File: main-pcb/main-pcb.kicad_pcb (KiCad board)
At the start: 10 copper layers, 118 x 90 mm, 443 parts, among them J1 CONN_01X03, J10 CONN_DUMPTRUCK_HOST, J11 CONN_01X03, J12 PMOD_HOST, J13 PMOD_HOST, J14 USB_C_Receptacle_USB2.0, J2 CORTEX_DEBUG_ETM, J3 XILINX_JTAG, J4 CORTEX_DEBUG_ETM, J5 CONN_01X03, J6 0826-1G1T-23-F, J7 CONN_DUMPTRUCK_HOST, J8 CONN_DUMPTRUCK_HOST, J9 CONN_DUMPTRUCK_HOST, M1 MECHANICAL, M2 SCREWHOLE, M3 SCREWHOLE, M4 SCREWHOLE, M5 SCREWHOLE, M6 MECHANICAL, M7 MECHANICAL, M8 MECHANICAL, M9 MECHANICAL, Q1 SSM6N58NU, SW1 SWITCH, SW2 SWITCH, U1 XC7S100-1FGGA484C, U10 NCP45525IMNTWG-H, U11 LTC3374-QFN, U12 AT24MAC402, U13 ECS-1612MV-250-CN, U14 STM32H735-UFBGA176-25, U15 S27KL0642GABHB020, U16 ECS-1612MV-250-CN, U17 S27KS0642GABHI030, U18 ECS-1612MV-250-CN, U19 INA230, U2 STM32L431-QFN48, U20 KSZ9031RN, U21 RCLAMP0514M, U22 RCLAMP0514M, U23 NCP45525IMNTWG-H, U24 IS25WP256D-JLLE, U25 INA230, U26 74LVC1T45, U27 NCP45525IMNTWG-H, U28 INA230, U29 NCP45525IMNTWG-H, U3 INA230, U30 INA230, U31 NCP45525IMNTWG-H, U32 INA230, U33 19-C47/RSGHBHC-5V01/2T, U34 19-C47/RSGHBHC-5V01/2T, U35 19-C47/RSGHBHC-5V01/2T, U36 19-C47/RSGHBHC-5V01/2T, U37 19-C47/RSGHBHC-5V01/2T, U38 19-C47/RSGHBHC-5V01/2T, U39 NCP45525IMNTWG-H, U4 INA230, U5 INA230, U6 INA230, U7 INA230, U8 INA230, U9 INA230

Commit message: 1088 unrouted
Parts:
- moved C145 45.4 mm to (196.8, 76.5)
- moved C146 45.4 mm to (196.8, 78.0)
- moved C151 45.4 mm to (196.8, 79.5)
- moved C152 45.4 mm to (196.8, 81.0)
- moved C157 45.4 mm to (199.2, 75.0)
- moved C158 45.4 mm to (199.2, 76.5)
- moved C159 45.4 mm to (199.2, 78.0)
- moved C160 45.4 mm to (199.2, 79.5)
- moved C161 45.4 mm to (199.2, 81.0)
- moved R45 45.4 mm to (201.8, 76.5)
- moved R47 45.4 mm to (201.8, 78.0)
- moved R48 45.4 mm to (201.8, 79.5)
- moved R49 45.4 mm to (201.8, 81.0)
- moved R54 45.4 mm to (204.2, 75.0)
- moved R55 45.4 mm to (204.2, 76.5)
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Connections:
- U1 pad A10: /2V5 VCCIO socket/DUT_GPIO4 -> /2V5 VCCIO socket/DUT_GPIO32
- U1 pad A2: /2V5 VCCIO socket/DUT_GPIO30 -> /2V5 VCCIO socket/DUT_GPIO25
- U1 pad A3: /2V5 VCCIO socket/DUT_GPIO28 -> /2V5 VCCIO socket/DUT_GPIO21
- U1 pad A4: /2V5 VCCIO socket/DUT_GPIO27 -> /2V5 VCCIO socket/DUT_GPIO24
- U1 pad A5: /2V5 VCCIO socket/DUT_GPIO26 -> /2V5 VCCIO socket/DUT_GPIO28
- U1 pad A6: /2V5 VCCIO socket/DUT_GPIO8 -> /2V5 VCCIO socket/DUT_GPIO46
- U1 pad A7: /2V5 VCCIO socket/DUT_GPIO7 -> /2V5 VCCIO socket/DUT_GPIO42
- U1 pad A9: /2V5 VCCIO socket/DUT_GPIO2 -> /2V5 VCCIO socket/DUT_GPIO36
- U1 pad B1: /2V5 VCCIO socket/DUT_GPIO34 -> /2V5 VCCIO socket/DUT_GPIO47
- U1 pad B10: /2V5 VCCIO socket/DUT_GPIO3 -> /2V5 VCCIO socket/DUT_GPIO30
- U1 pad B2: /2V5 VCCIO socket/DUT_GPIO33 -> /2V5 VCCIO socket/DUT_GPIO49
- U1 pad B3: /2V5 VCCIO socket/DUT_GPIO29 -> /2V5 VCCIO socket/DUT_GPIO23
- U1 pad B6: /2V5 VCCIO socket/DUT_GPIO25 -> /2V5 VCCIO socket/DUT_GPIO44
- U1 pad B7: /2V5 VCCIO socket/DUT_GPIO10 -> /2V5 VCCIO socket/DUT_GPIO40
- U1 pad B8: /2V5 VCCIO socket/DUT_GPIO9 -> /2V5 VCCIO socket/DUT_GPIO38
- U1 pad B9: /2V5 VCCIO socket/DUT_GPIO1 -> /2V5 VCCIO socket/DUT_GPIO34
- U1 pad C1: /2V5 VCCIO socket/DUT_GPIO36 -> /2V5 VCCIO socket/DUT_GPIO43
- U1 pad C2: /2V5 VCCIO socket/DUT_GPIO35 -> /2V5 VCCIO socket/DUT_GPIO45
- U1 pad C3: /2V5 VCCIO socket/DUT_GPIO32 -> /2V5 VCCIO socket/DUT_GPIO22
- U1 pad C4: /2V5 VCCIO socket/DUT_GPIO31 -> /2V5 VCCIO socket/DUT_GPIO26
- U1 pad C5: /2V5 VCCIO socket/DUT_GPIO14 -> /2V5 VCCIO socket/DUT_GPIO48
- U1 pad C6: /2V5 VCCIO socket/DUT_GPIO13 -> /2V5 VCCIO socket/DUT_GPIO10
- U1 pad C8: /2V5 VCCIO socket/DUT_GPIO6 -> /2V5 VCCIO socket/DUT_GPIO16
- U1 pad C9: /2V5 VCCIO socket/DUT_GPIO5 -> /2V5 VCCIO socket/DUT_GPIO20
- U1 pad D1: /2V5 VCCIO socket/DUT_GPIO48 -> /2V5 VCCIO socket/DUT_GPIO39
- U1 pad D2: /2V5 VCCIO socket/DUT_GPIO46 -> /2V5 VCCIO socket/DUT_GPIO41
- U1 pad D4: /2V5 VCCIO socket/DUT_GPIO40 -> /2V5 VCCIO socket/DUT_GPIO15
- U1 pad D5: /2V5 VCCIO socket/DUT_GPIO16 -> /2V5 VCCIO socket/DUT_GPIO17
- U1 pad D6: /2V5 VCCIO socket/DUT_GPIO15 -> /2V5 VCCIO socket/DUT_GPIO8
- U1 pad D8: /2V5 VCCIO socket/DUT_GPIO11 -> /2V5 VCCIO socket/DUT_GPIO14
- U1 pad E1: /2V5 VCCIO socket/DUT_GPIO42 -> /2V5 VCCIO socket/DUT_GPIO35
- U1 pad E2: /2V5 VCCIO socket/DUT_GPIO47 -> /2V5 VCCIO socket/DUT_GPIO33
- U1 pad E3: /2V5 VCCIO socket/DUT_GPIO45 -> /2V5 VCCIO socket/DUT_GPIO37
- U1 pad E4: /2V5 VCCIO socket/DUT_GPIO39 -> /2V5 VCCIO socket/DUT_GPIO11
- U1 pad E5: /2V5 VCCIO socket/DUT_GPIO20 -> /2V5 VCCIO socket/DUT_GPIO13
- U1 pad E8: /2V5 VCCIO socket/DUT_GPIO0 -> /2V5 VCCIO socket/DUT_GPIO18
- U1 pad F1: /2V5 VCCIO socket/DUT_GPIO41 -> /2V5 VCCIO socket/DUT_GPIO31
- U1 pad F4: /2V5 VCCIO socket/DUT_GPIO49 -> /2V5 VCCIO socket/DUT_GPIO9
- U1 pad F6: /2V5 VCCIO socket/DUT_GPIO24 -> /2V5 VCCIO socket/DUT_GPIO4
- U1 pad F7: /2V5 VCCIO socket/DUT_GPIO23 -> /2V5 VCCIO socket/DUT_GPIO2
- U1 pad F8: /2V5 VCCIO socket/DUT_GPIO18 -> /2V5 VCCIO socket/DUT_GPIO0
- U1 pad G1: /2V5 VCCIO socket/DUT_GPIO44 -> /2V5 VCCIO socket/DUT_GPIO27
- U1 pad G2: /2V5 VCCIO socket/DUT_GPIO43 -> /2V5 VCCIO socket/DUT_GPIO29
- U1 pad G3: /2V5 VCCIO socket/DUT_GPIO38 -> /2V5 VCCIO socket/DUT_GPIO5
- U1 pad G4: /2V5 VCCIO socket/DUT_GPIO37 -> /2V5 VCCIO socket/DUT_GPIO7
- U1 pad G6: /2V5 VCCIO socket/DUT_GPIO22 -> /2V5 VCCIO socket/DUT_GPIO3
- U1 pad G7: /2V5 VCCIO socket/DUT_GPIO21 -> /2V5 VCCIO socket/DUT_GPIO1
- U1 pad G8: /2V5 VCCIO socket/DUT_GPIO17 -> /2V5 VCCIO socket/DUT_GPIO6
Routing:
- net /2V5 VCCIO socket/DUT_GPIO18: track 0.00 -> 42.8 mm, vias 0 -> 2
- net /2V5 VCCIO socket/DUT_GPIO8: track 1.00 -> 43.6 mm, vias 0 -> 2
- net /2V5 VCCIO socket/DUT_GPIO30: track 1.00 -> 43.0 mm
- net /2V5 VCCIO socket/DUT_GPIO3: track 2.71 -> 44.4 mm, vias 0 -> 2
- net /2V5 VCCIO socket/DUT_GPIO10: track 2.46 -> 42.2 mm, vias 0 -> 2
- net /2V5 VCCIO socket/DUT_GPIO12: track 2.96 -> 42.5 mm, vias 1 -> 2
- net /2V5 VCCIO socket/DUT_GPIO14: track 3.21 -> 42.5 mm, vias 0 -> 2
- net /2V5 VCCIO socket/DUT_GPIO7: track 1.00 -> 39.6 mm, vias 0 -> 2
- net /2V5 VCCIO socket/DUT_GPIO5: track 3.25 -> 40.3 mm, vias 1 -> 2
- net /2V5 VCCIO socket/DUT_GPIO32: track 3.21 -> 39.8 mm
- net /2V5 VCCIO socket/DUT_GPIO16: track 4.66 -> 41.1 mm, vias 1 -> 2
- net /2V5 VCCIO socket/DUT_GPIO20: track 4.71 -> 40.7 mm, vias 1 -> 2
- net /2V5 VCCIO socket/DUT_GPIO9: track 2.71 -> 38.4 mm, vias 0 -> 2
- net /2V5 VCCIO socket/DUT_GPIO13: track 1.75 -> 36.6 mm, vias 1 -> 2
- net /2V5 VCCIO socket/DUT_GPIO17: track 0.00 -> 34.7 mm, vias 0 -> 2
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
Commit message: Continued routing
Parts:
- C20, C39: moved to B.Cu
- moved C178 172.4 mm to (23.2, 38.4)
- moved C179 172.4 mm to (27.0, 37.2)
- moved C180 172.4 mm to (27.0, 38.8)
- moved C181 172.4 mm to (27.0, 40.2)
- moved C182 172.4 mm to (23.2, 42.3)
- moved R94 172.4 mm to (27.0, 41.8)
- moved R95 172.4 mm to (27.0, 43.2)
- moved U23 172.4 mm to (30.1, 42.9)
- moved U25 172.4 mm to (30.6, 38.9)
- moved U36 135.8 mm to (31.7, 100.0)
- moved C204 130.1 mm to (31.4, 96.7)
- moved C209 123.8 mm to (73.2, 89.2), turned to -90 degrees
- moved TP13 123.7 mm to (59.8, 90.2)
- moved C210 120.6 mm to (76.5, 88.0), turned to 180 degrees
- moved C211 114.5 mm to (81.5, 95.8), turned to -135 degrees
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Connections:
- U1 pad F6: /2V5 VCCIO socket/DUT_GPIO4 -> /2V5 VCCIO socket/DUT_GPIO2
- U1 pad F7: /2V5 VCCIO socket/DUT_GPIO2 -> /2V5 VCCIO socket/DUT_GPIO4
- U1 pad F8: /2V5 VCCIO socket/DUT_GPIO0 -> /2V5 VCCIO socket/DUT_GPIO6
- U1 pad G8: /2V5 VCCIO socket/DUT_GPIO6 -> /2V5 VCCIO socket/DUT_GPIO0
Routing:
- net /GND: track 863.3 -> 934.1 mm, vias 233 -> 266
- net /2V5 VCCIO socket/DUT_GPIO0: track 0.00 -> 49.3 mm, vias 0 -> 2
- net /2V5 VCCIO socket/DUT_GPIO4: track 0.00 -> 46.2 mm, vias 0 -> 2
- net /2V5 VCCIO socket/DUT_GPIO2: track 0.00 -> 46.1 mm, vias 0 -> 2
- net /2V5 VCCIO socket/DUT_GPIO6: track 0.00 -> 46.0 mm, vias 0 -> 2
- net /2V5 VCCIO socket/DUT_GPIO1: track 0.00 -> 45.3 mm, vias 0 -> 2
- net /1V2: track 99.4 -> 119.2 mm, vias 8 -> 14
- net /1V0: track 64.7 -> 75.8 mm, vias 16 -> 28
- net /2V5: track 31.4 -> 38.5 mm, vias 4 -> 6
- net /1V8: track 164.1 -> 169.8 mm, vias 36 -> 43
- net /3V3: track 225.5 -> 230.9 mm, vias 15 -> 17
- net /2V5 VCCIO socket/DUT_GPIO20: track 40.7 -> 42.2 mm
- net /2V5 VCCIO socket/DUT_GPIO18: track 42.8 -> 44.3 mm
- net /Ethernet/FPGA_RAM_DQ6: track 19.2 -> 17.9 mm
- net /Ethernet/FPGA_RAM_DQ7: track 15.6 -> 14.6 mm
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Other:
- board text added: "1.2V IO"
- board text added: "1.8V IO"
- board text added: "1V2"
- board text added: "2.5V IO"
- board text added: "3.3V IO"
- board text added: "3V3"
- board text added: "FPGA JTAG"
- board text added: "FPGA PMOD"
- board text added: "GND"
- board text added: "MCU BOOT0"
- board text added: "MCU I2C"
- board text added: "MCU JTAG"
- board text added: "MCU PMOD"
- board text added: "MCU UART"
- board text added: "RX"
- board text added: "SCL"
- board text added: "SDA"
- board text added: "SUPER JTAG"
- board text added: "SUPER UART"
- board text added: "TX"
- board text added: "USB PWR 5V 900 mA"

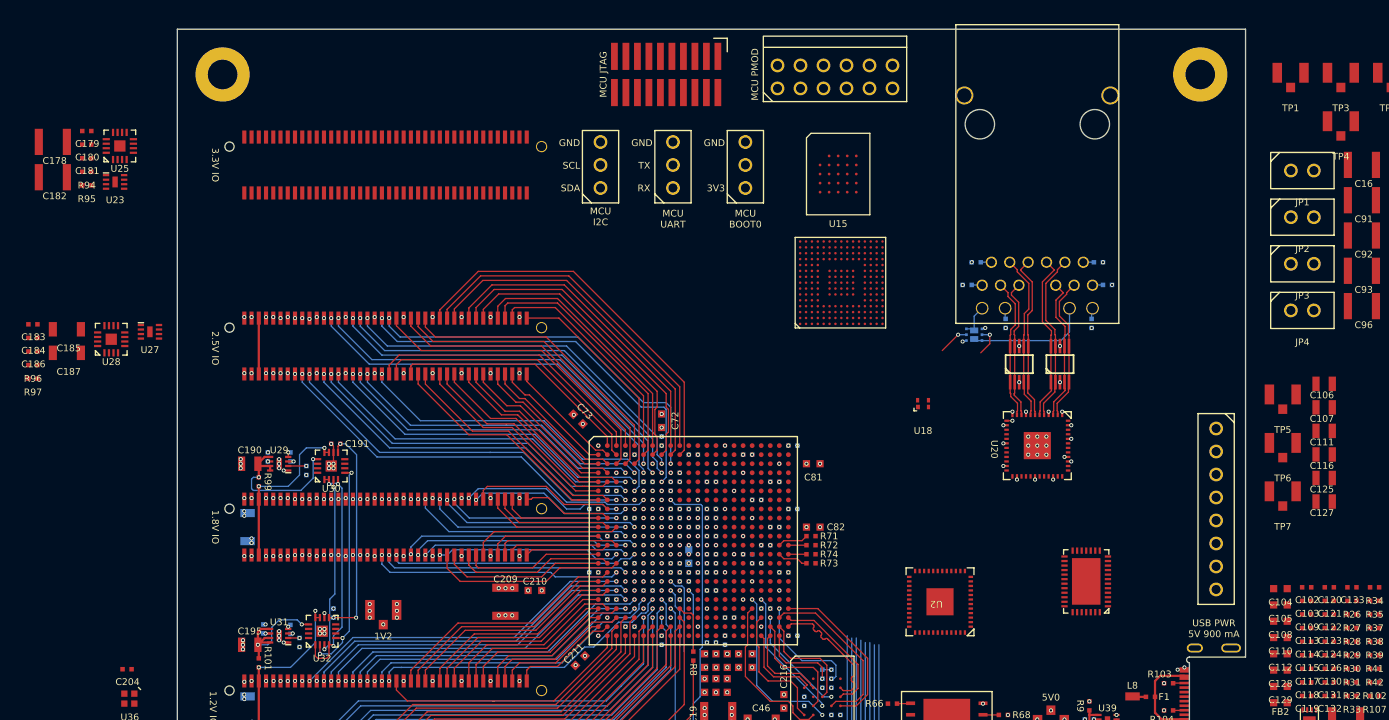
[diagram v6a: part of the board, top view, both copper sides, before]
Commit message: Continued routing 3V3 DUT socket
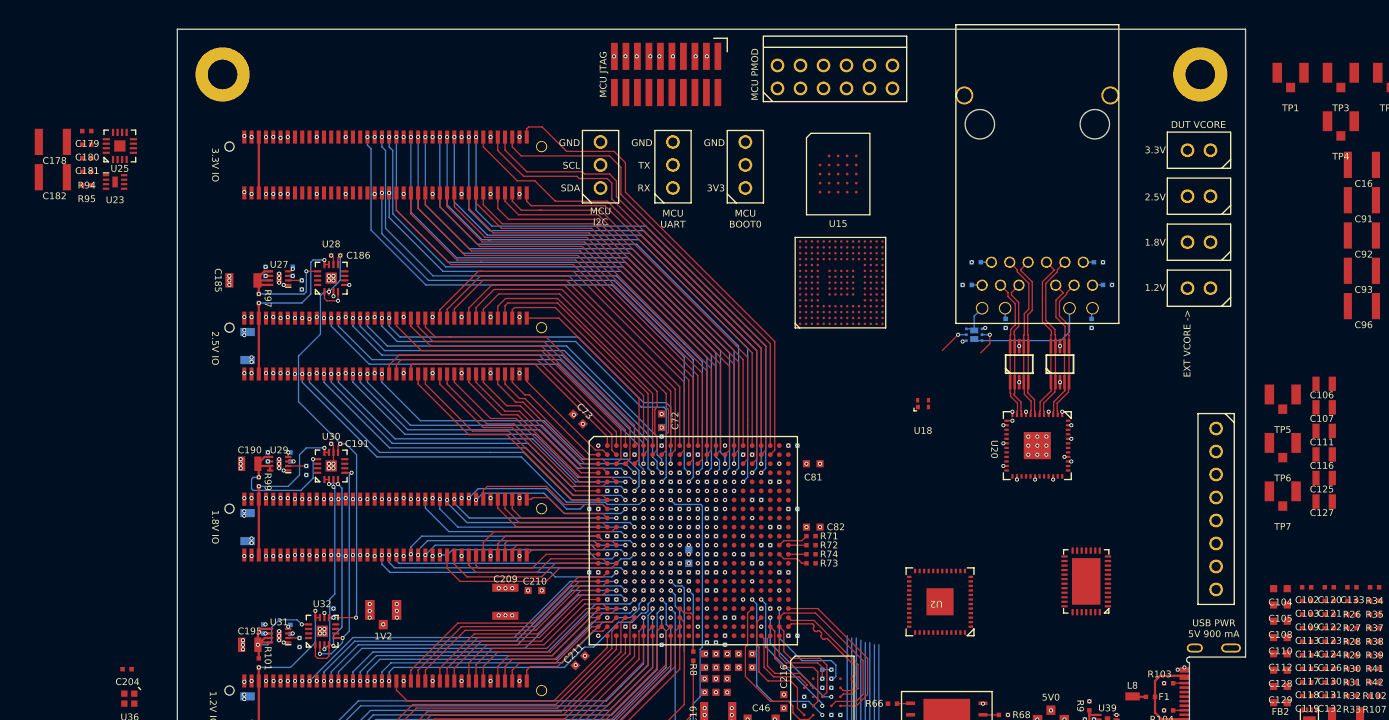
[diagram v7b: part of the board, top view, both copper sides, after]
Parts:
- C183, C184, C187, R96: moved to B.Cu
- moved C186 35.1 mm to (54.5, 51.0), turned to 180 degrees
- moved R96 31.0 mm to (50.8, 54.2), turned to -90 degrees
- moved C183 29.3 mm to (49.8, 52.8), turned to 90 degrees
- moved C184 26.7 mm to (46.8, 52.8), turned to 90 degrees
- moved R97 26.5 mm to (46.0, 55.8), turned to 90 degrees
- moved U28 25.2 mm to (54.0, 53.5)
- moved C185 20.2 mm to (44.3, 53.8), turned to 180 degrees
- moved C187 20.0 mm to (44.8, 61.0), turned to -90 degrees
- moved U27 15.5 mm to (48.2, 53.5), turned to 180 degrees
- moved JP4 11.7 mm to (149.9, 54.6), turned to 180 degrees
- moved JP3 11.7 mm to (149.9, 49.5), turned to 180 degrees
- moved JP2 11.7 mm to (149.9, 44.5), turned to 180 degrees
- moved JP1 11.6 mm to (149.9, 39.4), turned to 180 degrees
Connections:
- U1 pad A11: /3V3 VCCIO socket/DUT_GPIO15 -> /3V3 VCCIO socket/DUT_GPIO23
- U1 pad A12: /3V3 VCCIO socket/DUT_GPIO16 -> /3V3 VCCIO socket/DUT_GPIO27
- U1 pad A13: /3V3 VCCIO socket/DUT_GPIO18 -> /3V3 VCCIO socket/DUT_GPIO31
- U1 pad A14: /3V3 VCCIO socket/DUT_GPIO34 -> /3V3 VCCIO socket/DUT_GPIO35
- U1 pad A16: /3V3 VCCIO socket/DUT_GPIO35 -> /3V3 VCCIO socket/DUT_GPIO41
- U1 pad A17: /3V3 VCCIO socket/DUT_GPIO36 -> /3V3 VCCIO socket/DUT_GPIO45
- U1 pad A18: /3V3 VCCIO socket/DUT_GPIO41 -> /3V3 VCCIO socket/DUT_GPIO49
- U1 pad B13: /3V3 VCCIO socket/DUT_GPIO17 -> /3V3 VCCIO socket/DUT_GPIO33
- U1 pad B14: /3V3 VCCIO socket/DUT_GPIO33 -> /3V3 VCCIO socket/DUT_GPIO37
- U1 pad B15: /3V3 VCCIO socket/DUT_GPIO27 -> /3V3 VCCIO socket/DUT_GPIO39
- U1 pad B16: /3V3 VCCIO socket/DUT_GPIO28 -> /3V3 VCCIO socket/DUT_GPIO43
- U1 pad B19: /3V3 VCCIO socket/DUT_GPIO40 -> /3V3 VCCIO socket/DUT_GPIO44
- U1 pad B20: /3V3 VCCIO socket/DUT_GPIO45 -> /3V3 VCCIO socket/DUT_GPIO48
- U1 pad C10: /3V3 VCCIO socket/DUT_GPIO19 -> /3V3 VCCIO socket/DUT_GPIO5
- U1 pad C11: /3V3 VCCIO socket/DUT_GPIO20 -> /3V3 VCCIO socket/DUT_GPIO25
- U1 pad C12: /3V3 VCCIO socket/DUT_GPIO24 -> /3V3 VCCIO socket/DUT_GPIO29
- U1 pad C13: /3V3 VCCIO socket/DUT_GPIO14 -> /3V3 VCCIO socket/DUT_GPIO21
- U1 pad C15: /3V3 VCCIO socket/DUT_GPIO25 -> /3V3 VCCIO socket/DUT_GPIO24
- U1 pad C16: /3V3 VCCIO socket/DUT_GPIO26 -> /3V3 VCCIO socket/DUT_GPIO28
- U1 pad C17: /3V3 VCCIO socket/DUT_GPIO30 -> /3V3 VCCIO socket/DUT_GPIO47
- U1 pad C18: /3V3 VCCIO socket/DUT_GPIO38 -> /3V3 VCCIO socket/DUT_GPIO40
- U1 pad C19: /3V3 VCCIO socket/DUT_GPIO39 -> /3V3 VCCIO socket/DUT_GPIO36
- U1 pad D11: /3V3 VCCIO socket/DUT_GPIO6 -> /3V3 VCCIO socket/DUT_GPIO16
- U1 pad D12: /3V3 VCCIO socket/DUT_GPIO23 -> /3V3 VCCIO socket/DUT_GPIO18
- U1 pad D13: /3V3 VCCIO socket/DUT_GPIO13 -> /3V3 VCCIO socket/DUT_GPIO20
- U1 pad D14: /3V3 VCCIO socket/DUT_GPIO21 -> /3V3 VCCIO socket/DUT_GPIO22
- U1 pad D15: /3V3 VCCIO socket/DUT_GPIO22 -> /3V3 VCCIO socket/DUT_GPIO26
- U1 pad D16: /3V3 VCCIO socket/DUT_GPIO29 -> /3V3 VCCIO socket/DUT_GPIO30
- U1 pad D18: /3V3 VCCIO socket/DUT_GPIO37 -> /3V3 VCCIO socket/DUT_GPIO34
- U1 pad D19: /3V3 VCCIO socket/DUT_GPIO48 -> /3V3 VCCIO socket/DUT_GPIO38
- U1 pad E11: /3V3 VCCIO socket/DUT_GPIO5 -> /3V3 VCCIO socket/DUT_GPIO19
- U1 pad E15: /3V3 VCCIO socket/DUT_GPIO31 -> /3V3 VCCIO socket/DUT_GPIO15
- U1 pad E16: /3V3 VCCIO socket/DUT_GPIO32 -> /3V3 VCCIO socket/DUT_GPIO14
- U1 pad E17: /3V3 VCCIO socket/DUT_GPIO43 -> /3V3 VCCIO socket/DUT_GPIO32
- U1 pad E18: /3V3 VCCIO socket/DUT_GPIO44 -> /3V3 VCCIO socket/DUT_GPIO6
- U1 pad E19: /3V3 VCCIO socket/DUT_GPIO47 -> /3V3 VCCIO socket/DUT_GPIO13
- U1 pad G15: /3V3 VCCIO socket/DUT_GPIO49 -> /3V3 VCCIO socket/DUT_GPIO17
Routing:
- net /GND: track 934.1 -> 1212.7 mm, vias 266 -> 309
- net /PRSNT_3V3: track 0.00 -> 85.7 mm, vias 0 -> 1
- net /3V3 VCCIO socket/DUT_GPIO18: track 0.00 -> 63.9 mm, vias 0 -> 2
- net /3V3 VCCIO socket/DUT_GPIO16: track 0.00 -> 63.8 mm, vias 0 -> 2
- net /3V3 VCCIO socket/DUT_GPIO22: track 0.00 -> 63.6 mm, vias 0 -> 2
- net /3V3 VCCIO socket/DUT_GPIO20: track 0.00 -> 63.5 mm, vias 0 -> 2
- net /3V3 VCCIO socket/DUT_GPIO32: track 0.00 -> 63.2 mm, vias 0 -> 2
- net /3V3 VCCIO socket/DUT_GPIO26: track 0.00 -> 62.3 mm, vias 0 -> 2
- net /3V3 VCCIO socket/DUT_GPIO24: track 0.00 -> 61.5 mm, vias 0 -> 2
- net /3V3 VCCIO socket/DUT_GPIO30: track 0.00 -> 61.3 mm, vias 0 -> 2
- net /3V3 VCCIO socket/DUT_GPIO34: track 0.00 -> 61.1 mm, vias 0 -> 2
- net /3V3 VCCIO socket/DUT_GPIO28: track 0.00 -> 60.8 mm, vias 0 -> 2
- net /3V3 VCCIO socket/DUT_GPIO38: track 0.00 -> 60.5 mm, vias 0 -> 2
- net /3V3 VCCIO socket/DUT_GPIO36: track 0.00 -> 59.4 mm, vias 0 -> 2
- net /3V3 VCCIO socket/DUT_GPIO19: track 0.00 -> 58.4 mm, vias 0 -> 2
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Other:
- board text added: "1.2V"
- board text added: "1.8V"
- board text added: "2.5V"
- board text added: "3.3V"
- board text added: "DUT VCORE"
- board text added: "EXT VCORE ->"
